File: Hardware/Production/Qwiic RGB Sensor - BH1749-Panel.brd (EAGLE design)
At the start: 97.3 x 97.3 mm, 471 parts, among them J1 SMD, J10 PTH, J11 SMD, J13 SMD, J14 PTH, J15 SMD, J17 SMD, J18 PTH, J19 SMD, J2 SMD, J21 SMD, J22 PTH, J23 SMD, J25 SMD, J26 PTH, J27 SMD, J29 SMD, J3 PTH, J30 PTH, J31 SMD, J33 SMD, J34 PTH, J35 SMD, J4 SMD, J6 PTH, J7 SMD, J9 SMD, U1 BH1749NUC, U10 PCA9536, U11 BH1749NUC, U12 PCA9536, U13 BH1749NUC, U14 PCA9536, U15 BH1749NUC, U16 PCA9536, U17 BH1749NUC, U18 PCA9536, U2 PCA9536, U3 BH1749NUC, U4 PCA9536, U5 BH1749NUC, U6 PCA9536, U7 BH1749NUC, U8 PCA9536, U9 BH1749NUC

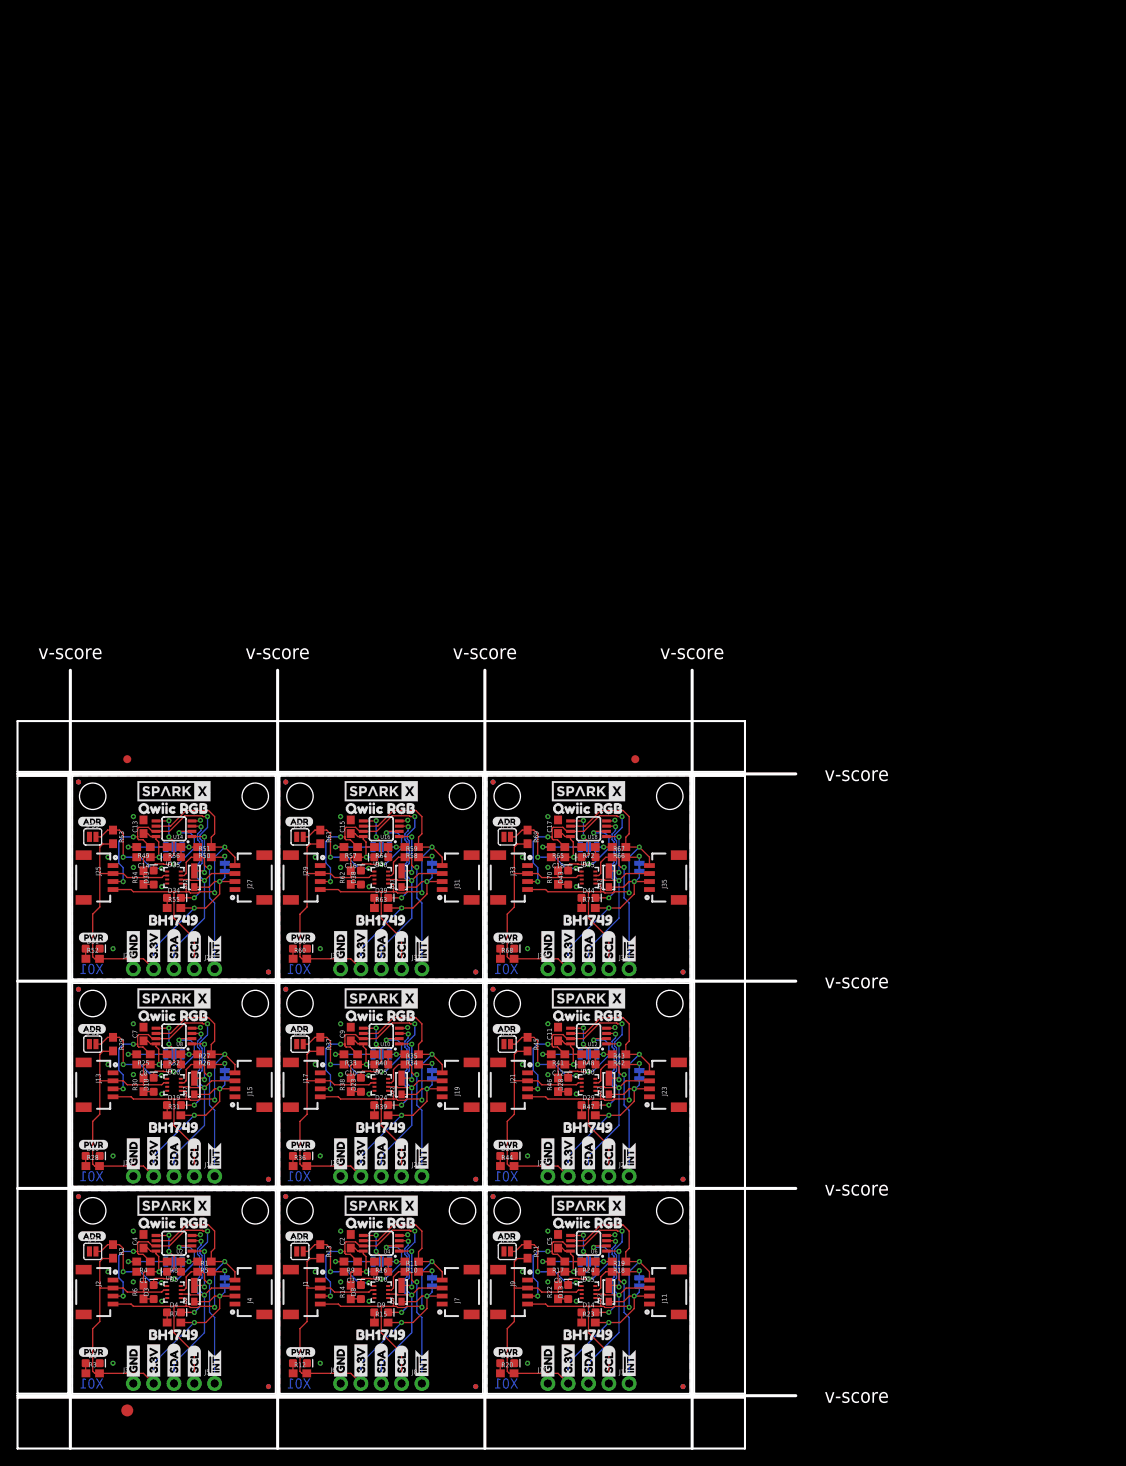
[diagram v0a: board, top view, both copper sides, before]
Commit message: Adding larger panel.
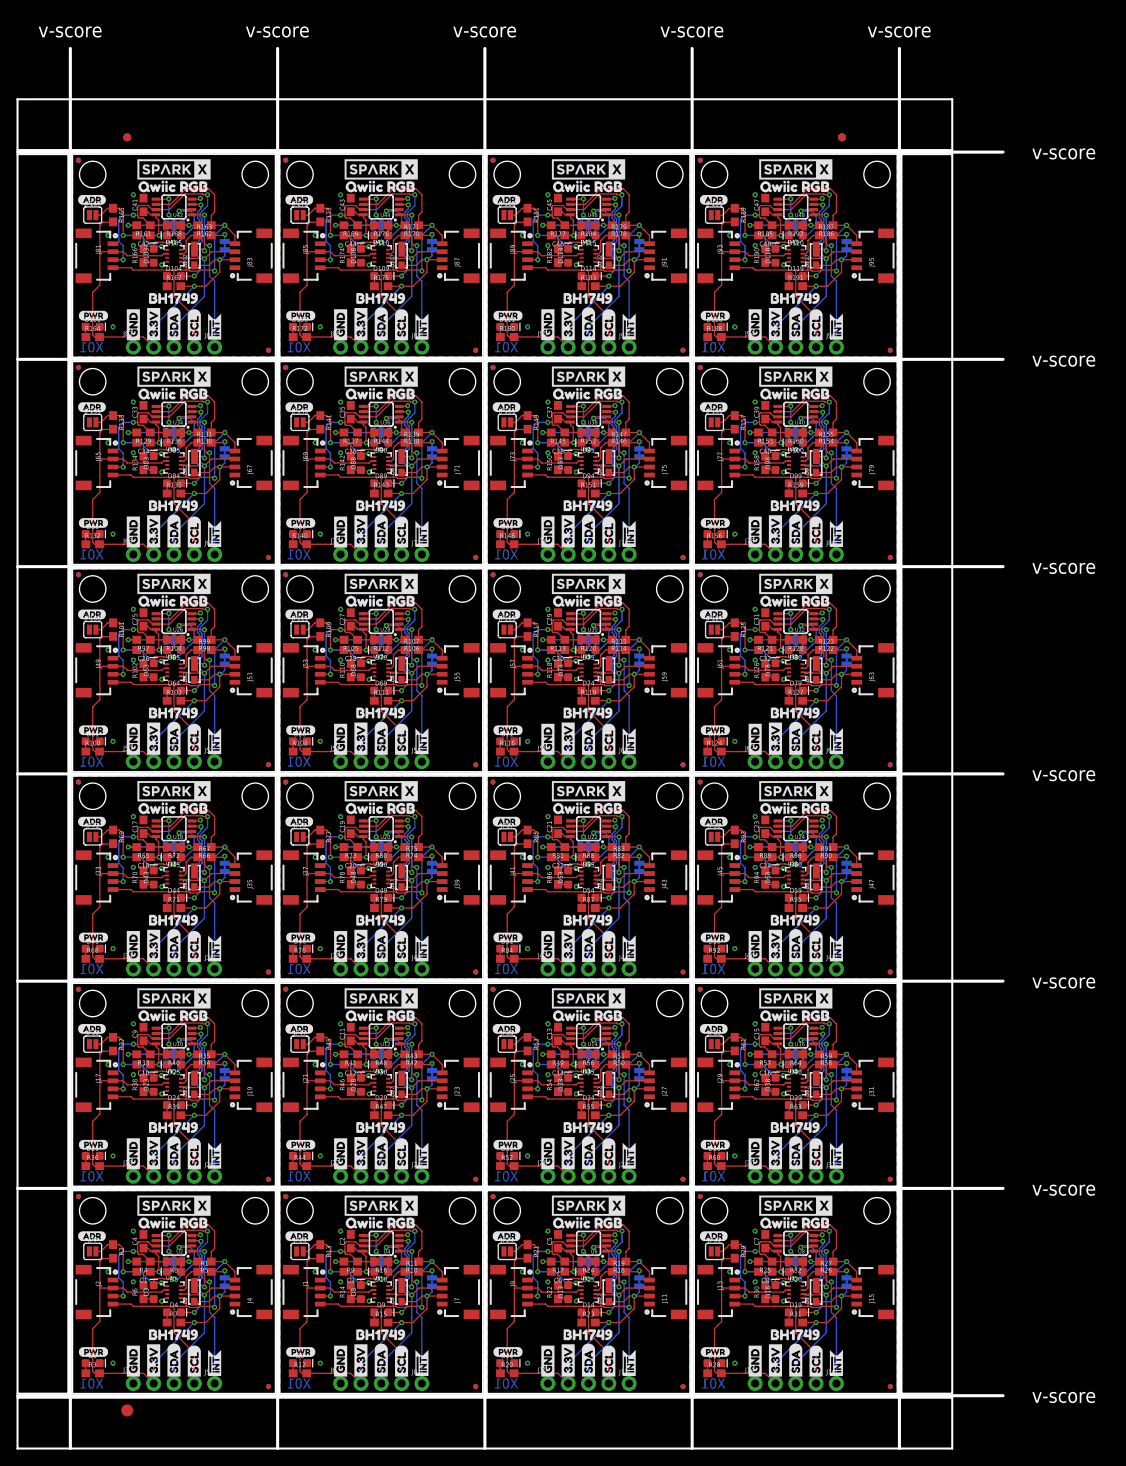
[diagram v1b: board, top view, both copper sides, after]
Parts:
- added C19, C20, C21, C22, C23, C24, C25, C26, C27, C28, C29, C30, C31, C32, C33, C34, C35, C36, C37, C38, C39, C40, C41, C42, C43, C44, C45, C46, C47, C48: 0.1uF, SparkFun-Capacitors:0603
- added D100, D105, D110, D115, D120, D50, D55, D60, D65, D70, D75, D80, D85, D90, D95: BLUE, SparkFun-LED:LED-0603
- added D101, D103, D106, D108, D111, D113, D116, D118, D46, D48, D51, D53, D56, D58, D61, D63, D66, D68, D71, D73, D76, D78, D81, D83, D86, D88, D91, D93, D96, D98: RED, SparkFun-LED:LED-0603
- added D102, D107, D112, D117, D47, D52, D57, D62, D67, D72, D77, D82, D87, D92, D97: 5700k, SparkX:SUPER_BRIGHT_SMD_LED_1206
- added D104, D109, D114, D119, D49, D54, D59, D64, D69, D74, D79, D84, D89, D94, D99: GREEN, SparkFun-LED:LED-0603
- added E$4: (no value), SparkFun-Aesthetics:FIDUCIAL-1X2
- added E$5: (no value), SparkFun-Retired:FIDUCIAL-1.5X3
- added I2C10, I2C11, I2C12, I2C13, I2C14, I2C15, I2C16, I2C17, I2C18, I2C19, I2C20, I2C21, I2C22, I2C23, I2C9: (no value), SparkFun-Jumpers:SMT-JUMPER_3_2-NC_TRACE_SILK
- added J37, J39, J41, J43, J45, J47, J49, J51, J53, J55, J57, J59, J61, J63, J65, J67, J69, J71, J73, J75, J77, J79, J81, J83, J85, J87, J89, J91, J93, J95: SMD, SparkX:1X04_1MM_RA
- added J38, J42, J46, J50, J54, J58, J62, J66, J70, J74, J78, J82, J86, J90, J94: PTH, SparkX:1X04_NO_SILK
- added J40, J44, J48, J52, J56, J60, J64, J68, J72, J76, J80, J84, J88, J92, J96: (no value), SparkFun-Connectors:1X01_NO_SILK
- added JP100, JP101, JP102, JP107, JP108, JP109, JP110, JP115, JP116, JP117, JP118, JP123, JP124, JP125, JP126, JP131, JP132, JP133, JP134, JP139, JP140, JP141, JP142, JP147, JP148, JP149, JP150, JP155, JP156, JP157, JP158, JP163, JP164, JP165, JP166, JP171, JP172, JP173, JP174, JP179, JP180, JP181, JP182, JP187, JP188, JP189, JP190, JP75, JP76, JP77, JP78, JP83, JP84, JP85, JP86, JP91, JP92, JP93, JP94, JP99: FIDUCIALUFIDUCIAL, SparkFun:MICRO-FIDUCIAL
- added JP103, JP111, JP119, JP127, JP135, JP143, JP151, JP159, JP167, JP175, JP183, JP191, JP79, JP87, JP95: ADR, SparkFun-Jumpers:SMT-JUMPER_2_NO_SILK
- added JP104, JP112, JP120, JP128, JP136, JP144, JP152, JP160, JP168, JP176, JP184, JP192, JP80, JP88, JP96: INT, SparkFun-Jumpers:SMT-JUMPER_2_NC_TRACE_SILK
- added JP105, JP106, JP113, JP114, JP121, JP122, JP129, JP130, JP137, JP138, JP145, JP146, JP153, JP154, JP161, JP162, JP169, JP170, JP177, JP178, JP185, JP186, JP73, JP74, JP81, JP82, JP89, JP90, JP97, JP98: STAND-OFF, SparkFun:STAND-OFF
- added LOGO10, LOGO11, LOGO12, LOGO13, LOGO14, LOGO15, LOGO16, LOGO17, LOGO18, LOGO19, LOGO20, LOGO21, LOGO22, LOGO23, LOGO24: OSHW-LOGOMINI, SparkFun-Aesthetics:OSHW-LOGO-MINI
- added R100, R108, R116, R124, R132, R140, R148, R156, R164, R172, R180, R188, R76, R84, R92: 1k, SparkFun-Resistors:0603
- added R101, R107, R109, R115, R117, R123, R125, R131, R133, R139, R141, R147, R149, R155, R157, R163, R165, R171, R173, R179, R181, R187, R189, R75, R77, R83, R85, R91, R93, R99: 10k, SparkFun-Resistors:0603
- added R102, R103, R104, R110, R111, R112, R118, R119, R120, R126, R127, R128, R134, R135, R136, R142, R143, R144, R150, R151, R152, R158, R159, R160, R166, R167, R168, R174, R175, R176, R182, R183, R184, R190, R191, R192, R78, R79, R80, R86, R87, R88, R94, R95, R96: 330, SparkFun-Resistors:0603
- added R105, R106, R113, R114, R121, R122, R129, R130, R137, R138, R145, R146, R153, R154, R161, R162, R169, R170, R177, R178, R185, R186, R73, R74, R81, R82, R89, R90, R97, R98: 2.2k, SparkFun-Resistors:0603
- added U$190, U$191, U$211, U$212, U$232, U$233, U$253, U$254, U$274, U$275, U$295, U$296, U$316, U$317, U$337, U$338, U$358, U$359, U$379, U$380, U$400, U$401, U$421, U$422, U$442, U$443, U$463, U$464, U$484, U$485: SPARKX-LOGO4, SparkX:SPARKX-MEDIUM
- added U$192, U$197, U$213, U$218, U$234, U$239, U$255, U$260, U$276, U$281, U$297, U$302, U$318, U$323, U$339, U$344, U$360, U$365, U$381, U$386, U$402, U$407, U$423, U$428, U$444, U$449, U$465, U$470, U$486, U$491: (no value), Labels-0_04:3#3V2
- added U$193, U$196, U$214, U$217, U$235, U$238, U$256, U$259, U$277, U$280, U$298, U$301, U$319, U$322, U$340, U$343, U$361, U$364, U$382, U$385, U$403, U$406, U$424, U$427, U$445, U$448, U$466, U$469, U$487, U$490: (no value), Labels-0_04:GND1
- added U$194, U$199, U$215, U$220, U$236, U$241, U$257, U$262, U$278, U$283, U$299, U$304, U$320, U$325, U$341, U$346, U$362, U$367, U$383, U$388, U$404, U$409, U$425, U$430, U$446, U$451, U$467, U$472, U$488, U$493: (no value), Labels-0_04:SCL9
- added U$195, U$198, U$216, U$219, U$237, U$240, U$258, U$261, U$279, U$282, U$300, U$303, U$321, U$324, U$342, U$345, U$363, U$366, U$384, U$387, U$405, U$408, U$426, U$429, U$447, U$450, U$468, U$471, U$489, U$492: (no value), Labels-0_04:SDA8
- added U$200, U$221, U$242, U$263, U$284, U$305, U$326, U$347, U$368, U$389, U$410, U$431, U$452, U$473, U$494: (no value), Labels:QWIIC-LOGO-MEDIUM
- added U$201, U$202, U$222, U$223, U$243, U$244, U$264, U$265, U$285, U$286, U$306, U$307, U$327, U$328, U$348, U$349, U$369, U$370, U$390, U$391, U$411, U$412, U$432, U$433, U$453, U$454, U$474, U$475, U$495, U$496: (no value), Labels:INT#-[<
- added U$203, U$224, U$245, U$266, U$287, U$308, U$329, U$350, U$371, U$392, U$413, U$434, U$455, U$476, U$497: (no value), Labels:PWR-()-03
- added U$204, U$225, U$246, U$267, U$288, U$309, U$330, U$351, U$372, U$393, U$414, U$435, U$456, U$477, U$498: (no value), Labels:ADR-()-03
- added U$205, U$226, U$247, U$268, U$289, U$310, U$331, U$352, U$373, U$394, U$415, U$436, U$457, U$478, U$499: (no value), Labels:I_SUPER2_C-()-03
- added U$206, U$210, U$227, U$231, U$248, U$252, U$269, U$273, U$290, U$294, U$311, U$315, U$332, U$336, U$353, U$357, U$374, U$378, U$395, U$399, U$416, U$420, U$437, U$441, U$458, U$462, U$479, U$483, U$500, U$504: (no value), buzzard_labels (23):BH17493
- added U$207, U$228, U$249, U$270, U$291, U$312, U$333, U$354, U$375, U$396, U$417, U$438, U$459, U$480, U$501: (no value), buzzard_labels (23):INT0
- added U$208, U$209, U$229, U$230, U$250, U$251, U$271, U$272, U$292, U$293, U$313, U$314, U$334, U$335, U$355, U$356, U$376, U$377, U$397, U$398, U$418, U$419, U$439, U$440, U$460, U$461, U$481, U$482, U$502, U$503: (no value), buzzard_labels (23):QWIIC_RGB2
- added U19, U21, U23, U25, U27, U29, U31, U33, U35, U37, U39, U41, U43, U45, U47: BH1749NUC, BH1749NUC:BH1749NUC
- added U20, U22, U24, U26, U28, U30, U32, U34, U36, U38, U40, U42, U44, U46, U48: PCA9536, PCA9536:MSOP8
- E$3: device SparkFun-Retired:FIDUCIAL-1.5X3 -> SparkFun-Aesthetics:FIDUCIAL-1X2
- moved E$3 182.5 mm to (96.2, 157.0)
- moved E$2 100.4 mm to (6.86, 157.0), flipped to the bottom
- moved C7 81.9 mm to (86.6, 19.1)
- moved C8 81.9 mm to (86.6, 15.2)
- moved D17 81.9 mm to (93.0, 12.7)
- moved D18 81.9 mm to (87.9, 12.7)
- moved D19 81.9 mm to (90.4, 10.2)
- moved D20 81.9 mm to (90.4, 15.2)
- moved I2C3 81.9 mm to (90.4, 16.5)
- moved J13 81.9 mm to (82.8, 12.7)
- moved J16 81.9 mm to (95.5, 1.27)
- moved JP26 81.9 mm to (100.6, 22.9)
- moved JP27 81.9 mm to (102.2, 0.89)
- moved JP28 81.9 mm to (78.5, 24.6)
- moved JP29 81.9 mm to (78.5, 24.6)
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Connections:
- new net !INT10: J44.1, R83.1, U21.7
- new net !INT11: J48.1, R91.1, U23.7
- new net !INT12: J52.1, R99.1, U25.7
- new net !INT13: J56.1, R107.1, U27.7
- new net !INT14: J60.1, R115.1, U29.7
- new net !INT15: J64.1, R123.1, U31.7
- new net !INT16: J68.1, R131.1, U33.7
- new net !INT17: J72.1, R139.1, U35.7
- new net !INT18: J76.1, R147.1, U37.7
- new net !INT19: J80.1, R155.1, U39.7
- new net !INT20: J84.1, R163.1, U41.7
- new net !INT21: J88.1, R171.1, U43.7
- new net !INT22: J92.1, R179.1, U45.7
- new net !INT23: J96.1, R187.1, U47.7
- new net !INT9: J40.1, R75.1, U19.7
- new net 3.3V10: C21.1, C22.1, D52.A, I2C10.2, J41.2, J42.2, J43.2, JP88.2, R84.2, R85.2, R86.2, R87.2, R88.2, U21.2, U22.8
- new net 3.3V11: C23.1, C24.1, D57.A, I2C11.2, J45.2, J46.2, J47.2, JP96.2, R92.2, R93.2, R94.2, R95.2, R96.2, U23.2, U24.8
- new net 3.3V12: C25.1, C26.1, D62.A, I2C12.2, J49.2, J50.2, J51.2, JP104.2, R100.2, R101.2, R102.2, R103.2, R104.2, U25.2, U26.8
- new net 3.3V13: C27.1, C28.1, D67.A, I2C13.2, J53.2, J54.2, J55.2, JP112.2, R108.2, R109.2, R110.2, R111.2, R112.2, U27.2, U28.8
- new net 3.3V14: C29.1, C30.1, D72.A, I2C14.2, J57.2, J58.2, J59.2, JP120.2, R116.2, R117.2, R118.2, R119.2, R120.2, U29.2, U30.8
- new net 3.3V15: C31.1, C32.1, D77.A, I2C15.2, J61.2, J62.2, J63.2, JP128.2, R124.2, R125.2, R126.2, R127.2, R128.2, U31.2, U32.8
- new net 3.3V16: C33.1, C34.1, D82.A, I2C16.2, J65.2, J66.2, J67.2, JP136.2, R132.2, R133.2, R134.2, R135.2, R136.2, U33.2, U34.8
- new net 3.3V17: C35.1, C36.1, D87.A, I2C17.2, J69.2, J70.2, J71.2, JP144.2, R140.2, R141.2, R142.2, R143.2, R144.2, U35.2, U36.8
- new net 3.3V18: C37.1, C38.1, D92.A, I2C18.2, J73.2, J74.2, J75.2, JP152.2, R148.2, R149.2, R150.2, R151.2, R152.2, U37.2, U38.8
- new net 3.3V19: C39.1, C40.1, D97.A, I2C19.2, J77.2, J78.2, J79.2, JP160.2, R156.2, R157.2, R158.2, R159.2, R160.2, U39.2, U40.8
- new net 3.3V20: C41.1, C42.1, D102.A, I2C20.2, J81.2, J82.2, J83.2, JP168.2, R164.2, R165.2, R166.2, R167.2, R168.2, U41.2, U42.8
- new net 3.3V21: C43.1, C44.1, D107.A, I2C21.2, J85.2, J86.2, J87.2, JP176.2, R172.2, R173.2, R174.2, R175.2, R176.2, U43.2, U44.8
- new net 3.3V22: C45.1, C46.1, D112.A, I2C22.2, J89.2, J90.2, J91.2, JP184.2, R180.2, R181.2, R182.2, R183.2, R184.2, U45.2, U46.8
- new net 3.3V23: C47.1, C48.1, D117.A, I2C23.2, J93.2, J94.2, J95.2, JP192.2, R188.2, R189.2, R190.2, R191.2, R192.2, U47.2, U48.8
- new net 3.3V9: C19.1, C20.1, D47.A, I2C9.2, J37.2, J38.2, J39.2, JP80.2, R76.2, R77.2, R78.2, R79.2, R80.2, U19.2, U20.8
- new net ADR10: JP87.2, R85.1, U21.1
- new net ADR11: JP95.2, R93.1, U23.1
- new net ADR12: JP103.2, R101.1, U25.1
- new net ADR13: JP111.2, R109.1, U27.1
- new net ADR14: JP119.2, R117.1, U29.1
- new net ADR15: JP127.2, R125.1, U31.1
- new net ADR16: JP135.2, R133.1, U33.1
- new net ADR17: JP143.2, R141.1, U35.1
- new net ADR18: JP151.2, R149.1, U37.1
- new net ADR19: JP159.2, R157.1, U39.1
- new net ADR20: JP167.2, R165.1, U41.1
- new net ADR21: JP175.2, R173.1, U43.1
- new net ADR22: JP183.2, R181.1, U45.1
- new net ADR23: JP191.2, R189.1, U47.1
- new net ADR9: JP79.2, R77.1, U19.1
- new net GND10: C21.2, C22.2, D51.C, J41.1, J42.1, J43.1, JP87.1, U21.3, U21.4, U22.4
- new net GND11: C23.2, C24.2, D56.C, J45.1, J46.1, J47.1, JP95.1, U23.3, U23.4, U24.4
- new net GND12: C25.2, C26.2, D61.C, J49.1, J50.1, J51.1, JP103.1, U25.3, U25.4, U26.4
- new net GND13: C27.2, C28.2, D66.C, J53.1, J54.1, J55.1, JP111.1, U27.3, U27.4, U28.4
- new net GND14: C29.2, C30.2, D71.C, J57.1, J58.1, J59.1, JP119.1, U29.3, U29.4, U30.4
- new net GND15: C31.2, C32.2, D76.C, J61.1, J62.1, J63.1, JP127.1, U31.3, U31.4, U32.4
- new net GND16: C33.2, C34.2, D81.C, J65.1, J66.1, J67.1, JP135.1, U33.3, U33.4, U34.4
- new net GND17: C35.2, C36.2, D86.C, J69.1, J70.1, J71.1, JP143.1, U35.3, U35.4, U36.4
- new net GND18: C37.2, C38.2, D91.C, J73.1, J74.1, J75.1, JP151.1, U37.3, U37.4, U38.4
- new net GND19: C39.2, C40.2, D96.C, J77.1, J78.1, J79.1, JP159.1, U39.3, U39.4, U40.4
- new net GND20: C41.2, C42.2, D101.C, J81.1, J82.1, J83.1, JP167.1, U41.3, U41.4, U42.4
- new net GND21: C43.2, C44.2, D106.C, J85.1, J86.1, J87.1, JP175.1, U43.3, U43.4, U44.4
- new net GND22: C45.2, C46.2, D111.C, J89.1, J90.1, J91.1, JP183.1, U45.3, U45.4, U46.4
- new net GND23: C47.2, C48.2, D116.C, J93.1, J94.1, J95.1, JP191.1, U47.3, U47.4, U48.4
- new net GND9: C19.2, C20.2, D46.C, J37.1, J38.1, J39.1, JP79.1, U19.3, U19.4, U20.4
- new net N$100: I2C9.1, R74.2
- new net N$101: I2C9.3, R73.2
- new net N$102: JP80.1, R75.2
- new net N$103: D46.A, R76.1
- new net N$104: D47.C, U20.1
- new net N$105: D48.C, U20.2
- new net N$106: D49.C, U20.3
- new net N$107: D50.C, U20.5
- new net N$108: D48.A, R78.1
- new net N$109: D49.A, R79.1
- new net N$110: D50.A, R80.1
- new net N$111: I2C10.1, R82.2
- new net N$112: I2C10.3, R81.2
- new net N$113: JP88.1, R83.2
- new net N$114: D51.A, R84.1
- new net N$115: D52.C, U22.1
- new net N$116: D53.C, U22.2
- new net N$117: D54.C, U22.3
- new net N$118: D55.C, U22.5
- new net N$119: D53.A, R86.1
- new net N$120: D54.A, R87.1
- new net N$121: D55.A, R88.1
- new net N$122: I2C11.1, R90.2
- new net N$123: I2C11.3, R89.2
- new net N$124: JP96.1, R91.2
- new net N$125: D56.A, R92.1
- new net N$126: D57.C, U24.1
- new net N$127: D58.C, U24.2
- new net N$128: D59.C, U24.3
- new net N$129: D60.C, U24.5
- new net N$130: D58.A, R94.1
- new net N$131: D59.A, R95.1
- new net N$132: D60.A, R96.1
- new net N$133: I2C12.1, R98.2
- new net N$134: I2C12.3, R97.2
- new net N$135: JP104.1, R99.2
- new net N$136: D61.A, R100.1
- new net N$137: D62.C, U26.1
- new net N$138: D63.C, U26.2
- new net N$139: D64.C, U26.3
- new net N$140: D65.C, U26.5
- new net N$141: D63.A, R102.1
- new net N$142: D64.A, R103.1
- new net N$143: D65.A, R104.1
- new net N$144: I2C13.1, R106.2
- new net N$145: I2C13.3, R105.2
- new net N$146: JP112.1, R107.2
- new net N$147: D66.A, R108.1
- new net N$148: D67.C, U28.1
- new net N$149: D68.C, U28.2
- new net N$150: D69.C, U28.3
- new net N$151: D70.C, U28.5
- new net N$152: D68.A, R110.1
- new net N$153: D69.A, R111.1
- new net N$154: D70.A, R112.1
- new net N$155: I2C14.1, R114.2
- new net N$156: I2C14.3, R113.2
- new net N$157: JP120.1, R115.2
- new net N$158: D71.A, R116.1
- new net N$159: D72.C, U30.1
- new net N$160: D73.C, U30.2
- new net N$161: D74.C, U30.3
- new net N$162: D75.C, U30.5
- new net N$163: D73.A, R118.1
- new net N$164: D74.A, R119.1
- new net N$165: D75.A, R120.1
- new net N$166: I2C15.1, R122.2
- new net N$167: I2C15.3, R121.2
- new net N$168: JP128.1, R123.2
- new net N$169: D76.A, R124.1
- new net N$170: D77.C, U32.1
- new net N$171: D78.C, U32.2
- new net N$172: D79.C, U32.3
- new net N$173: D80.C, U32.5
- new net N$174: D78.A, R126.1
- new net N$175: D79.A, R127.1
- new net N$176: D80.A, R128.1
- new net N$177: I2C16.1, R130.2
- new net N$178: I2C16.3, R129.2
- new net N$179: JP136.1, R131.2
- new net N$180: D81.A, R132.1
- new net N$181: D82.C, U34.1
- new net N$182: D83.C, U34.2
- new net N$183: D84.C, U34.3
- new net N$184: D85.C, U34.5
- new net N$185: D83.A, R134.1
- new net N$186: D84.A, R135.1
- new net N$187: D85.A, R136.1
- new net N$188: I2C17.1, R138.2
- new net N$189: I2C17.3, R137.2
- new net N$190: JP144.1, R139.2
- new net N$191: D86.A, R140.1
- new net N$192: D87.C, U36.1
- new net N$193: D88.C, U36.2
- new net N$194: D89.C, U36.3
- new net N$195: D90.C, U36.5
- new net N$196: D88.A, R142.1
- new net N$197: D89.A, R143.1
- new net N$198: D90.A, R144.1
- new net N$199: I2C18.1, R146.2
- new net N$200: I2C18.3, R145.2
- new net N$201: JP152.1, R147.2
- new net N$202: D91.A, R148.1
- new net N$203: D92.C, U38.1
- new net N$204: D93.C, U38.2
- new net N$205: D94.C, U38.3
- new net N$206: D95.C, U38.5
- new net N$207: D93.A, R150.1
- new net N$208: D94.A, R151.1
- new net N$209: D95.A, R152.1
- new net N$210: I2C19.1, R154.2
- new net N$211: I2C19.3, R153.2
- new net N$212: JP160.1, R155.2
- new net N$213: D96.A, R156.1
- new net N$214: D97.C, U40.1
- new net N$215: D98.C, U40.2
- new net N$216: D99.C, U40.3
- new net N$217: D100.C, U40.5
- new net N$218: D98.A, R158.1
- new net N$219: D99.A, R159.1
- new net N$220: D100.A, R160.1
- new net N$221: I2C20.1, R162.2
- new net N$222: I2C20.3, R161.2
- new net N$223: JP168.1, R163.2
- new net N$224: D101.A, R164.1
- new net N$225: D102.C, U42.1
- new net N$226: D103.C, U42.2
- new net N$227: D104.C, U42.3
- new net N$228: D105.C, U42.5
- new net N$229: D103.A, R166.1
- new net N$230: D104.A, R167.1
- new net N$231: D105.A, R168.1
- new net N$232: I2C21.1, R170.2
- new net N$233: I2C21.3, R169.2
- new net N$234: JP176.1, R171.2
- new net N$235: D106.A, R172.1
- new net N$236: D107.C, U44.1
- new net N$237: D108.C, U44.2
- new net N$238: D109.C, U44.3
- new net N$239: D110.C, U44.5
- new net N$240: D108.A, R174.1
- new net N$241: D109.A, R175.1
- new net N$242: D110.A, R176.1
- new net N$243: I2C22.1, R178.2
- new net N$244: I2C22.3, R177.2
- new net N$245: JP184.1, R179.2
- new net N$246: D111.A, R180.1
- new net N$247: D112.C, U46.1
- new net N$248: D113.C, U46.2
- new net N$249: D114.C, U46.3
- new net N$250: D115.C, U46.5
- new net N$251: D113.A, R182.1
- new net N$252: D114.A, R183.1
- new net N$253: D115.A, R184.1
- new net N$254: I2C23.1, R186.2
- new net N$255: I2C23.3, R185.2
- new net N$256: JP192.1, R187.2
- new net N$257: D116.A, R188.1
- new net N$258: D117.C, U48.1
- new net N$259: D118.C, U48.2
- new net N$260: D119.C, U48.3
- new net N$261: D120.C, U48.5
- new net N$262: D118.A, R190.1
- new net N$263: D119.A, R191.1
- new net N$264: D120.A, R192.1
- new net SCL10: J41.4, J42.4, J43.4, R82.1, U21.5, U22.6
- new net SCL11: J45.4, J46.4, J47.4, R90.1, U23.5, U24.6
- new net SCL12: J49.4, J50.4, J51.4, R98.1, U25.5, U26.6
- new net SCL13: J53.4, J54.4, J55.4, R106.1, U27.5, U28.6
- new net SCL14: J57.4, J58.4, J59.4, R114.1, U29.5, U30.6
- new net SCL15: J61.4, J62.4, J63.4, R122.1, U31.5, U32.6
- new net SCL16: J65.4, J66.4, J67.4, R130.1, U33.5, U34.6
- new net SCL17: J69.4, J70.4, J71.4, R138.1, U35.5, U36.6
- new net SCL18: J73.4, J74.4, J75.4, R146.1, U37.5, U38.6
- new net SCL19: J77.4, J78.4, J79.4, R154.1, U39.5, U40.6
- new net SCL20: J81.4, J82.4, J83.4, R162.1, U41.5, U42.6
- new net SCL21: J85.4, J86.4, J87.4, R170.1, U43.5, U44.6
- new net SCL22: J89.4, J90.4, J91.4, R178.1, U45.5, U46.6
- new net SCL23: J93.4, J94.4, J95.4, R186.1, U47.5, U48.6
- new net SCL9: J37.4, J38.4, J39.4, R74.1, U19.5, U20.6
- new net SDA10: J41.3, J42.3, J43.3, R81.1, U21.6, U22.7
- new net SDA11: J45.3, J46.3, J47.3, R89.1, U23.6, U24.7
- new net SDA12: J49.3, J50.3, J51.3, R97.1, U25.6, U26.7
- new net SDA13: J53.3, J54.3, J55.3, R105.1, U27.6, U28.7
- new net SDA14: J57.3, J58.3, J59.3, R113.1, U29.6, U30.7
- new net SDA15: J61.3, J62.3, J63.3, R121.1, U31.6, U32.7
- new net SDA16: J65.3, J66.3, J67.3, R129.1, U33.6, U34.7
- new net SDA17: J69.3, J70.3, J71.3, R137.1, U35.6, U36.7
- new net SDA18: J73.3, J74.3, J75.3, R145.1, U37.6, U38.7
- new net SDA19: J77.3, J78.3, J79.3, R153.1, U39.6, U40.7
- new net SDA20: J81.3, J82.3, J83.3, R161.1, U41.6, U42.7
- new net SDA21: J85.3, J86.3, J87.3, R169.1, U43.6, U44.7
- new net SDA22: J89.3, J90.3, J91.3, R177.1, U45.6, U46.7
- new net SDA23: J93.3, J94.3, J95.3, R185.1, U47.6, U48.7
- new net SDA9: J37.3, J38.3, J39.3, R73.1, U19.6, U20.7
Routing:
- net 3.3V23: track 0.00 -> 69.7 mm, vias 0 -> 3
- net 3.3V20: track 0.00 -> 69.7 mm, vias 0 -> 3
- net 3.3V22: track 0.00 -> 69.7 mm, vias 0 -> 3
- net 3.3V19: track 0.00 -> 69.7 mm, vias 0 -> 3
- net 3.3V18: track 0.00 -> 69.7 mm, vias 0 -> 3
- net 3.3V15: track 0.00 -> 69.7 mm, vias 0 -> 3
- net 3.3V14: track 0.00 -> 69.7 mm, vias 0 -> 3
- net 3.3V12: track 0.00 -> 69.7 mm, vias 0 -> 3
- net 3.3V11: track 0.00 -> 69.7 mm, vias 0 -> 3
- net 3.3V10: track 0.00 -> 69.7 mm, vias 0 -> 3
- net 3.3V9: track 0.00 -> 69.7 mm, vias 0 -> 3
- net 3.3V21: track 0.00 -> 69.7 mm, vias 0 -> 3
- net 3.3V17: track 0.00 -> 69.7 mm, vias 0 -> 3
- net 3.3V16: track 0.00 -> 69.7 mm, vias 0 -> 3
- net 3.3V13: track 0.00 -> 69.7 mm, vias 0 -> 3
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- added copper zone on layer 1, net GND10
- added copper zone on layer 16, net GND10
- added copper zone on layer 1, net GND11
- added copper zone on layer 16, net GND11
- added copper zone on layer 1, net GND12
- added copper zone on layer 16, net GND12
- added copper zone on layer 1, net GND13
- added copper zone on layer 16, net GND13
- added copper zone on layer 1, net GND14
- added copper zone on layer 16, net GND14
- added copper zone on layer 1, net GND15
- added copper zone on layer 16, net GND15
- added copper zone on layer 1, net GND16
- added copper zone on layer 16, net GND16
- added copper zone on layer 1, net GND17
- added copper zone on layer 16, net GND17
- added copper zone on layer 1, net GND18
- added copper zone on layer 16, net GND18
- added copper zone on layer 1, net GND19
- added copper zone on layer 16, net GND19
- added copper zone on layer 1, net GND20
- added copper zone on layer 16, net GND20
- added copper zone on layer 1, net GND21
- added copper zone on layer 16, net GND21
- added copper zone on layer 1, net GND22
- added copper zone on layer 16, net GND22
- added copper zone on layer 1, net GND23
- added copper zone on layer 16, net GND23
- added copper zone on layer 1, net GND9
- added copper zone on layer 16, net GND9
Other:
- board size 97.3 x 97.3 mm -> 123.2 x 175 mm
